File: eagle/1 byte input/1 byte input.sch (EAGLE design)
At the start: 15 parts, among them IC1 74LS165N, X3 MKDSN1,5/8-5,08

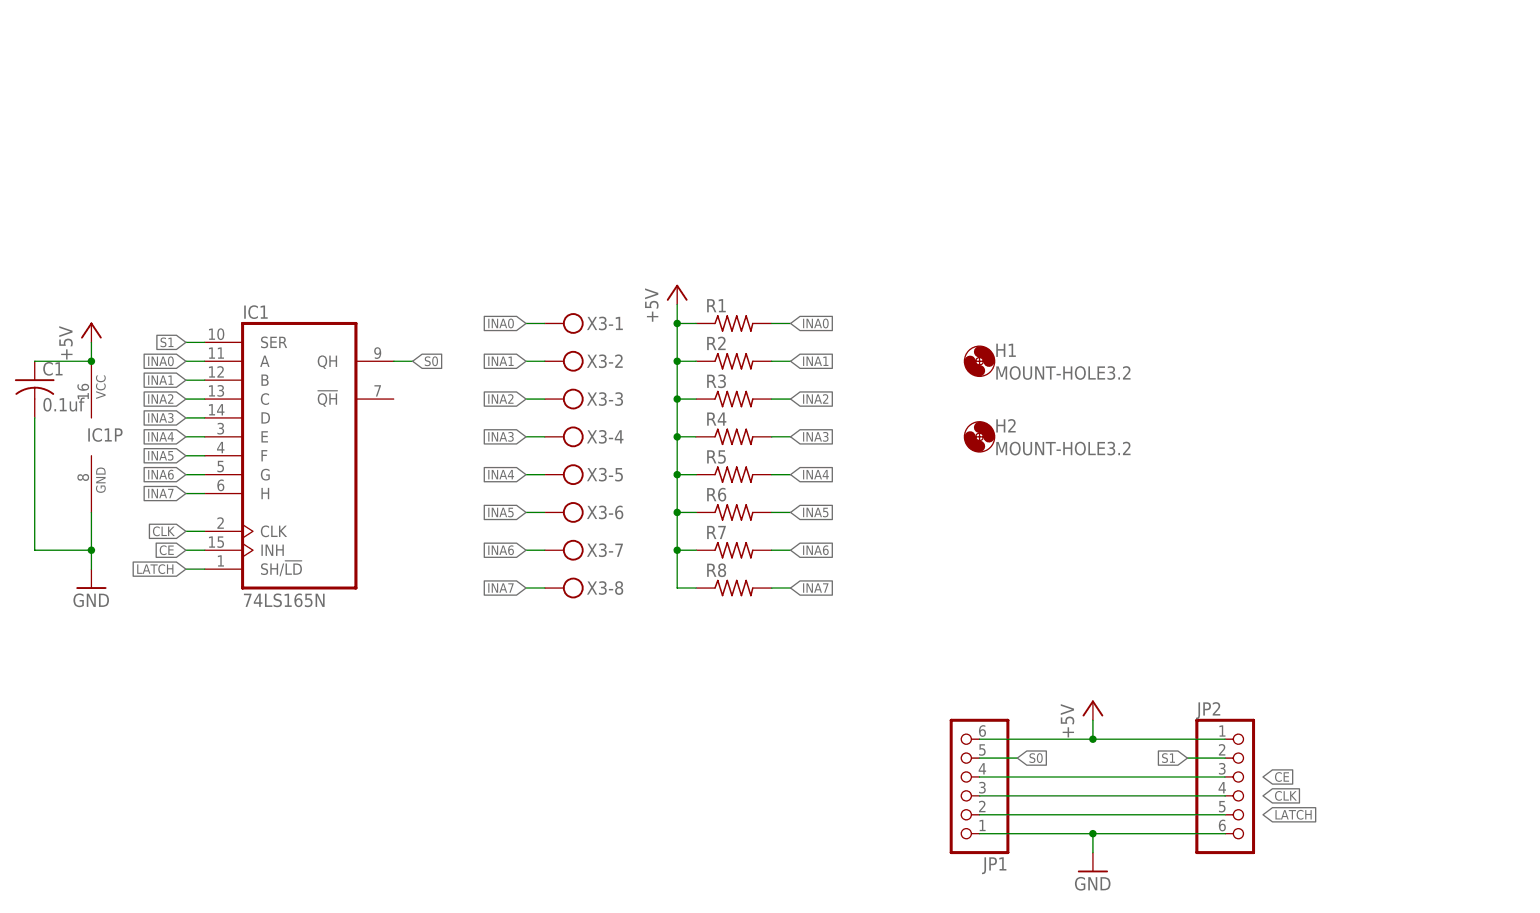
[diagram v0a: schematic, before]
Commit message: added pdf file of schematics and boards, removed button debounce and servo driver
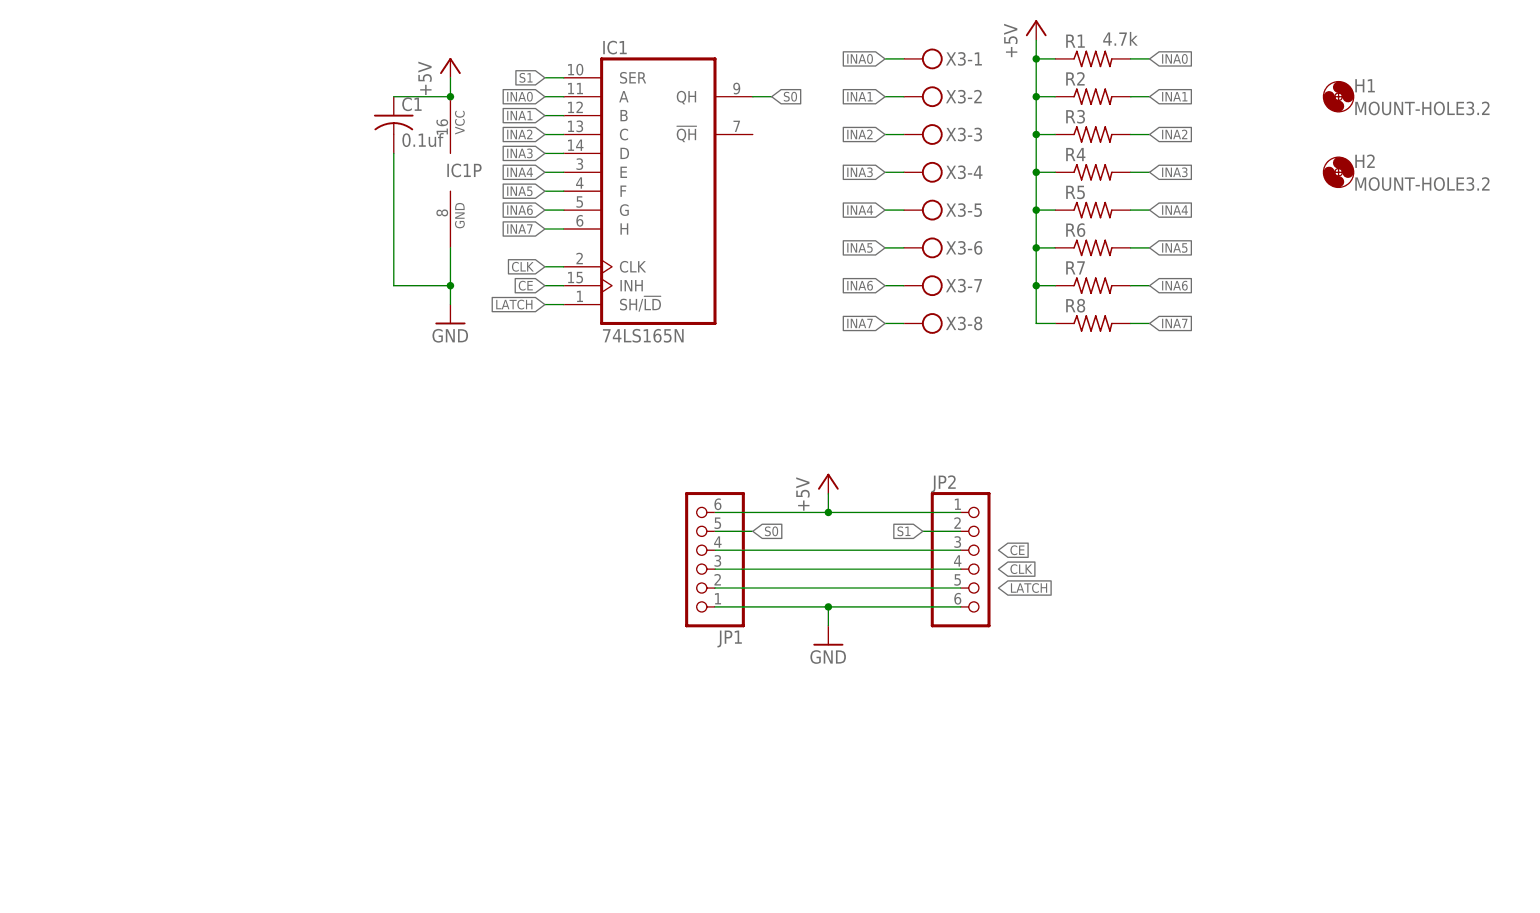
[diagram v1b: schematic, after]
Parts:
- R1: value (none) -> 4.7k
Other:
- moved on the sheet: C1, H1, H2, IC1, IC1P, JP1, JP2, R1, R2, R3, R4, R5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
